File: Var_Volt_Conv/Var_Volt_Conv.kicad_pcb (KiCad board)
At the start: 2 copper layers, 99 parts, among them J101 Jack-DC, J102 Screw_Terminal_01x02, J103 Screw_Terminal_01x02, J201 Conn_01x05, Q101 AO3416, Q102 IRFML8244TRPBF, Q103 IRFML8244TRPBF, Q104 AO3407, Q105 AO3407, Q106 AO3407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

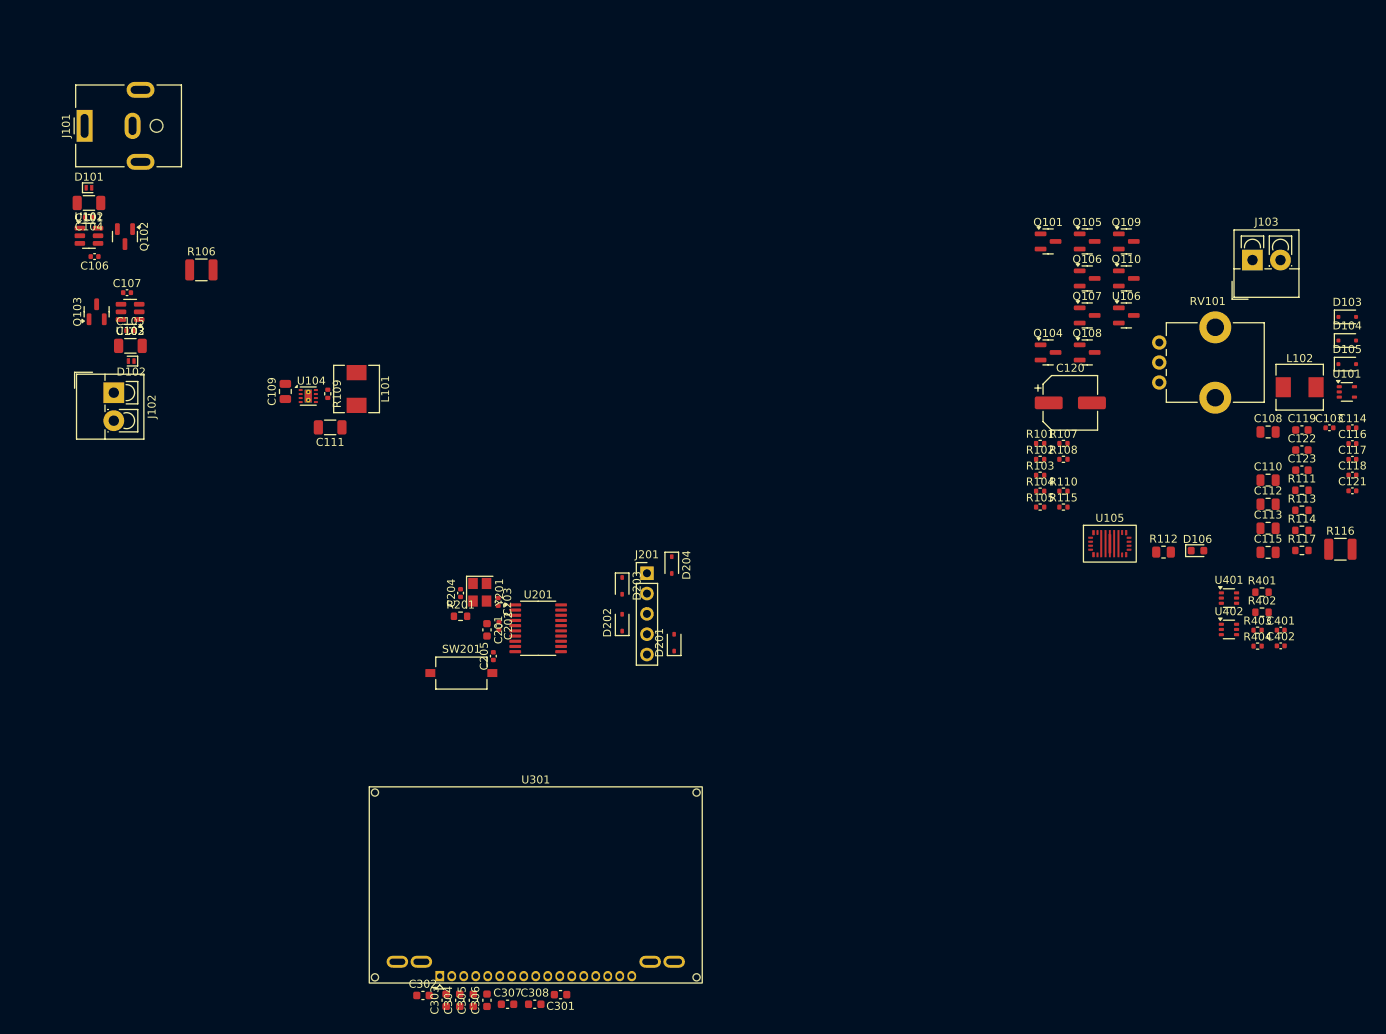
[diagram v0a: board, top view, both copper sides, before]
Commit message: Completed rough layout
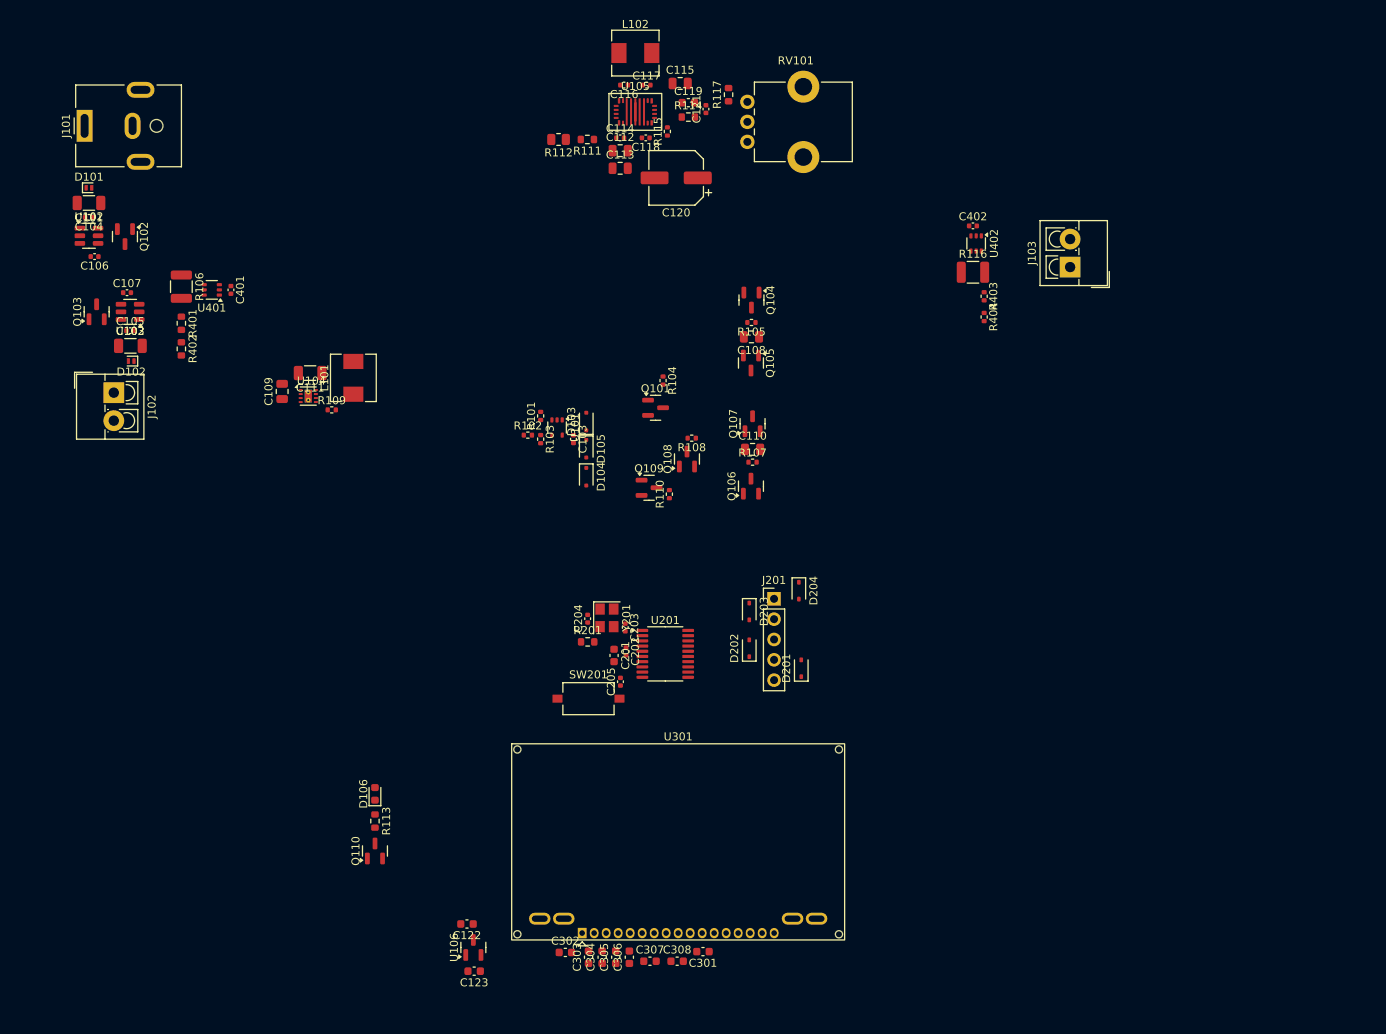
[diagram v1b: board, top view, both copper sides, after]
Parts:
- moved R401 139.2 mm to (39.0, 58.4), turned to -90 degrees
- moved R402 139.0 mm to (39.0, 61.6), turned to -90 degrees
- moved C401 137.9 mm to (45.2, 54.2), turned to -90 degrees
- moved U401 132.9 mm to (42.8, 54.2), turned to 180 degrees
- moved R113 122.2 mm to (63.2, 120.6), turned to -90 degrees
- moved C123 120.9 mm to (75.6, 139.4), turned to 180 degrees
- moved C122 120.0 mm to (74.7, 133.5), turned to 180 degrees
- moved Q110 118.1 mm to (63.2, 124.3), turned to 90 degrees
- moved U106 113.6 mm to (75.5, 136.4), turned to 90 degrees
- moved D106 107.2 mm to (63.2, 117.2), turned to 90 degrees
- moved C116 101.5 mm to (94.3, 28.6), turned to 180 degrees
- moved C117 99.9 mm to (97.2, 28.6)
- moved R111 99.5 mm to (89.8, 35.4), turned to 180 degrees
- moved U101 98.8 mm to (86.0, 71.4), turned to -90 degrees
- moved C114 98.4 mm to (93.8, 35.2)
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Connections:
- net /[1] Power/BUCK_3V3 renamed /[1] Power/BUCK_VOS
- net Net-(C121-Pad1) renamed /[1] Power/BB_COMP2
- net Net-(D103-K) renamed /[1] Power/COMP_POWER
- net Net-(D104-K) renamed /[1] Power/ST_3V3_Diode
- net Net-(D106-K) renamed /[1] Power/POW_IND_LED_R
- net Net-(Q101-D) renamed /[1] Power/BUCK_PPM_INV
- net Net-(Q104-G) renamed /[1] Power/BUCK_PPM_GATE
- net Net-(Q104-S) renamed /[1] Power/BUCK_PPM_SOURCE
- net Net-(Q106-G) renamed /[1] Power/ST_PPM_GATE
- net Net-(Q106-S) renamed /[1] Power/ST_PPM_SOURCE
- net Net-(Q108-D) renamed /[1] Power/ST_PPM_INV2
- net Net-(Q108-G) renamed /[1] Power/ST_PPM_INV1
- net Net-(Q110-D) renamed /[1] Power/POW_IND_R_NMOS
- net Net-(R111-Pad2) renamed /[1] Power/BB_FSW2
- net Net-(R117-Pad1) renamed /[1] Power/BB_POT_R
- net Net-(U101--) renamed /[1] Power/ST_PPM_IN
- net Net-(U102-VCAP) renamed /[1] Power/VCAP_J
- net Net-(U103-VCAP) renamed /[1] Power/VCAP_T
- net Net-(U104-PG) renamed /[1] Power/PG
- net Net-(U104-SW) renamed /[1] Power/BUCK_SW
- net Net-(U105-BOOT1) renamed /[1] Power/BB_BOOT1
- net Net-(U105-BOOT2) renamed /[1] Power/BB_BOOT2
- net Net-(U105-COMP) renamed /[1] Power/BB_COMP1
- net Net-(U105-FB) renamed /[1] Power/BB_FEEDBACK
- net Net-(U105-FSW) renamed /[1] Power/BB_FSW1
- net Net-(U105-SW1) renamed /[1] Power/BB_SW1
- net Net-(U105-SW2) renamed /[1] Power/BB_SW2
- net Net-(U201-PC14/PB9) renamed /[2] Microcontroller/HSE_IN
- net Net-(U301-C1+) renamed /[3] Display/LC1+
- net Net-(U301-C1-) renamed /[3] Display/LC1-
- net Net-(U301-C2+) renamed /[3] Display/LC2+
- net Net-(U301-C2-) renamed /[3] Display/LC2-
- net Net-(U301-V0) renamed /[3] Display/LV0
- net Net-(U301-V1) renamed /[3] Display/LV1
- net Net-(U301-V2) renamed /[3] Display/LV2
- net Net-(U301-V3) renamed /[3] Display/LV3
- net Net-(U301-V4) renamed /[3] Display/LV4
- net Net-(U301-VOUT) renamed /[3] Display/LVOUT
- C111 pad 2: Net-(U104-FB) -> GND
- C204 pad 2: Net-(C204-Pad2) -> /[2] Microcontroller/HSE_OUT
- U104 pad 5: Net-(U104-FB) -> GND
- U201 pad 3: Net-(U201-PC15) -> /[2] Microcontroller/HSE_OUT
- Y201 pad 1: Net-(C204-Pad2) -> /[2] Microcontroller/HSE_OUT

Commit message: Update design rules
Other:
- copper layers 2 -> 6
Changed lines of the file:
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@@
 	(generator_version "8.0")
 	(general
-		(thickness 1.6)
+		(thickness 1.5596)
 		(legacy_teardrops no)
 	)
@@
 	(layers
 		(0 "F.Cu" signal)
+		(1 "In1.Cu" power)
+		(2 "In2.Cu" power)
+		(3 "In3.Cu" power)
+		(4 "In4.Cu" power)
 		(31 "B.Cu" signal)
 		(32 "B.Adhes" user "B.Adhesive")
@@
 	)
 	(setup
+		(stackup
+			(layer "F.SilkS"
+				(type "Top Silk Screen")
+			)
+			(layer "F.Paste"
+				(type "Top Solder Paste")
+			)
+			(layer "F.Mask"
+				(type "Top Solder Mask")
+				(thickness 0.01)
+			)
+			(layer "F.Cu"
+				(type "copper")
+				(thickness 0.035)
+			)
+			(layer "dielectric 1"
+				(type "prepreg")
+				(thickness 0.1)
+				(material "FR4")
+				(epsilon_r 4.5)
+				(loss_tangent 0.02)
+			)
+			(layer "In1.Cu"
+				(type "copper")
+				(thickness 0.0152)
+			)
+			(layer "dielectric 2"
+				(type "core")
+				(thickness 0.55)
+				(material "FR4")
+				(epsilon_r 4.5)
+				(loss_tangent 0.02)
+			)
+			(layer "In2.Cu"
+				(type "copper")
+				(thickness 0.0152)
+			)
+			(layer "dielectric 3"
+				(type "prepreg")
+				(thickness 0.1088)
+				(material "FR4")
+				(epsilon_r 4.5)
+				(loss_tangent 0.02)
+			)
+			(layer "In3.Cu"
+				(type "copper")
+				(thickness 0.0152)
+			)
+			(layer "dielectric 4"
+				(type "core")
+				(thickness 0.55)
+				(material "FR4")
+				(epsilon_r 4.5)
+				(loss_tangent 0.02)
+			)
+			(layer "In4.Cu"
+				(type "copper")
+				(thickness 0.0152)
+			)
+			(layer "dielectric 5"
+				(type "prepreg")
+				(thickness 0.1)
+				(material "FR4")
+				(epsilon_r 4.5)
+				(loss_tangent 0.02)
+			)
+			(layer "B.Cu"
+				(type "copper")
+				(thickness 0.035)
+			)
+			(layer "B.Mask"
+				(type "Bottom Solder Mask")
+				(thickness 0.01)
+			)
+			(layer "B.Paste"
+				(type "Bottom Solder Paste")
+			)
+			(layer "B.SilkS"
+				(type "Bottom Silk Screen")
+			)
+			(copper_finish "None")
+			(dielectric_constraints no)
+		)
 		(pad_to_mask_clearance 0)
 		(allow_soldermask_bridges_in_footprints no)
@@
 		(tags "resistor")
 		(property "Reference" "R116"
-			(at 0 -2.28 360)
+			(at 0 -2.28 0)
 			(layer "F.SilkS")
 			(effects
@@
 		)
 		(property "Value" "11mR"
-			(at 0 2.28 360)
+			(at 0 2.28 0)
 			(layer "F.Fab")
 			(effects
@@
 		)
 		(fp_text user "${REFERENCE}"
-			(at 0 0 360)
+			(at 0 0 0)
 			(layer "F.Fab")
 			(effects
@@
 		(tags "capacitor")
 		(property "Reference" "C116"
-			(at 0 -1.16 360)
+			(at 0 -1.16 0)
 			(layer "F.SilkS")
 			(effects
@@
 		)
 		(property "Value" "0.1uF"
-			(at 0 1.16 360)
+			(at 0 1.16 0)
 			(layer "F.Fab")
 			(effects
@@
 		)
 		(fp_text user "${REFERENCE}"
-			(at 0 0 360)
+			(at 0 0 0)
 			(layer "F.Fab")
 			(effects
@@
 		(tags "capacitor")
 		(property "Reference" "C402"
-			(at 0 -1.16 360)
+			(at 0 -1.16 0)
 			(layer "F.SilkS")
 			(effects
@@
 		)
 		(property "Value" "0.1uF"
-			(at 0 1.16 360)
+			(at 0 1.16 0)
 			(layer "F.Fab")
 			(effects
@@
 		)
 		(fp_text user "${REFERENCE}"
-			(at 0 0 360)
+			(at 0 0 0)
 			(layer "F.Fab")
 			(effects
@@
 			(size 4 4)
 			(drill 2.2)
-			(layers "F&B.Cu" "*.Mask")
+			(layers "*.Cu" "*.Mask")
 		)
 		(pad "" np_thru_hole circle
@@
 			(size 4 4)
 			(drill 2.2)
-			(layers "F&B.Cu" "*.Mask")
+			(layers "*.Cu" "*.Mask")
 		)
 		(pad "1" thru_hole circle
@@
 		(tags "capacitor electrolytic")
 		(property "Reference" "C120"
-			(at 0 -4.35 360)
+			(at 0 -4.35 0)
 			(layer "F.SilkS")
 			(effects
@@
 		)
 		(property "Value" "100uF"
-			(at 0 4.35 360)
+			(at 0 4.35 0)
 			(layer "F.Fab")
 			(effects
@@
 		)
 		(fp_text user "${REFERENCE}"
-			(at 0 0 360)
+			(at 0 0 0)
 			(layer "F.Fab")
 			(effects
@@
 		(tags "capacitor")
 		(property "Reference" "C118"
-			(at 0 -1.16 360)
+			(at 0 -1.16 0)
 			(layer "F.SilkS")
 			(effects
@@
 		)
 		(property "Value" "0.1uF"
-			(at 0 1.16 360)
+			(at 0 1.16 0)
 			(layer "F.Fab")
 			(effects
@@
 		)
 		(fp_text user "${REFERENCE}"
-			(at 0 0 360)
+			(at 0 0 0)
 			(layer "F.Fab")
 			(effects
@@
 		)
 		(fp_text user "${REFERENCE}"
-			(at 0 0 360)
+			(at 0 0 0)
 			(layer "F.Fab")
 			(effects
@@
 		(tags "SOT TO_SOT_SMD")
 		(property "Reference" "Q101"
-			(at 0 -2.4 360)
+			(at 0 -2.4 0)
 			(layer "F.SilkS")
 			(effects
@@
 		)
 		(property "Value" "AO3416"
-			(at 0 2.4 360)
+			(at 0 2.4 0)
 			(layer "F.Fab")
 			(effects
@@
 		)
 		(fp_text user "${REFERENCE}"
-			(at 0 0 360)
+			(at 0 0 0)
 			(layer "F.Fab")
 			(effects
@@
 		(tags "resistor")
 		(property "Reference" "R112"
-			(at 0 -1.65 360)
+			(at 0 -1.65 0)
 			(layer "F.SilkS")
 			(effects
@@
 		)
 		(property "Value" "4.3k"
-			(at 0 1.65 360)
+			(at 0 1.65 0)
 			(layer "F.Fab")
 			(effects
@@
 		)
 		(fp_text user "${REFERENCE}"
-			(at 0 0 360)
+			(at 0 0 0)
 			(layer "F.Fab")
 			(effects
@@
 		(tags "capacitor")
 		(property "Reference" "C110"
-			(at 0 -1.68 360)
+			(at 0 -1.68 0)
 			(layer "F.SilkS")
 			(effects
@@
 		)
 		(property "Value" "10uF"
-			(at 0 1.68 360)
+			(at 0 1.68 0)
 			(layer "F.Fab")
 			(effects
@@
 		)
 		(fp_text user "${REFERENCE}"
-			(at 0 0 360)
+			(at 0 0 0)
 			(layer "F.Fab")
 			(effects
@@
 		(tags "resistor")
 		(property "Reference" "R108"
-			(at 0 -1.17 360)
+			(at 0 -1.17 0)
 			(layer "F.SilkS")
 			(effects
@@
 		)
 		(property "Value" "100k"
-			(at 0 1.17 360)
+			(at 0 1.17 0)
 			(layer "F.Fab")
 			(effects
@@
 		)
 		(fp_text user "${REFERENCE}"
-			(at 0 0 360)
+			(at 0 0 0)
 			(layer "F.Fab")
 			(effects
@@
 		(tags "resistor")
 		(property "Reference" "R105"
-			(at 0 -1.17 360)
+			(at 0 -1.17 0)
 			(layer "F.SilkS")
 			(effects
@@
 		)
 		(property "Value" "100k"
-			(at 0 1.17 360)
+			(at 0 1.17 0)
 			(layer "F.Fab")
 			(effects
@@
 		)
 		(fp_text user "${REFERENCE}"
-			(at 0 0 360)
+			(at 0 0 0)
 			(layer "F.Fab")
 			(effects
@@
 		(tags "capacitor")
 		(property "Reference" "C108"
-			(at 0 -1.68 360)
+			(at 0 -1.68 0)
 			(layer "F.SilkS")
 			(effects
@@
 		)
 		(property "Value" "10uF"
-			(at 0 1.68 360)
+			(at 0 1.68 0)
 			(layer "F.Fab")
 			(effects
@@
 		)
 		(fp_text user "${REFERENCE}"
-			(at 0 0 360)
+			(at 0 0 0)
 			(layer "F.Fab")
 			(effects
@@
 		(tags "SOT-363 SC-70-6")
 		(property "Reference" "U401"
-			(at 0 -2.25 360)
+			(at 0 -2.25 0)
 			(layer "F.SilkS")
 			(effects
@@
 		)
 		(property "Value" "INA215BIDCKR"
-			(at 0 2 360)
+			(at 0 2 0)
 			(layer "F.Fab")
 			(effects
@@
 		(tags "resistor")
 		(property "Reference" "R107"
-			(at 0 -1.17 360)
+			(at 0 -1.17 0)
 			(layer "F.SilkS")
 			(effects
@@
 		)
 		(property "Value" "100k"
-			(at 0 1.17 360)
+			(at 0 1.17 0)
 			(layer "F.Fab")
 			(effects
@@
 		)
 		(fp_text user "${REFERENCE}"
-			(at 0 0 360)
+			(at 0 0 0)
 			(layer "F.Fab")
 			(effects
@@
 		(tags "capacitor")
 		(property "Reference" "C117"
-			(at 0 -1.16 360)
+			(at 0 -1.16 0)
 			(layer "F.SilkS")
 			(effects
@@
 		)
 		(property "Value" "0.1uF"
-			(at 0 1.16 360)
+			(at 0 1.16 0)
 			(layer "F.Fab")
 			(effects
@@
 		)
 		(fp_text user "${REFERENCE}"
-			(at 0 0 360)
+			(at 0 0 0)
 			(layer "F.Fab")
 			(effects
@@
 		(tags "resistor")
 		(property "Reference" "R111"
-			(at 0 -1.43 360)
+			(at 0 -1.43 0)
 			(layer "F.SilkS")
 			(effects
@@
 		)
 		(property "Value" "5k"
-			(at 0 1.43 360)
+			(at 0 1.43 0)
 			(layer "F.Fab")
 			(effects
@@
 		)
 		(fp_text user "${REFERENCE}"
-			(at 0 0 360)
+			(at 0 0 0)
 			(layer "F.Fab")
 			(effects

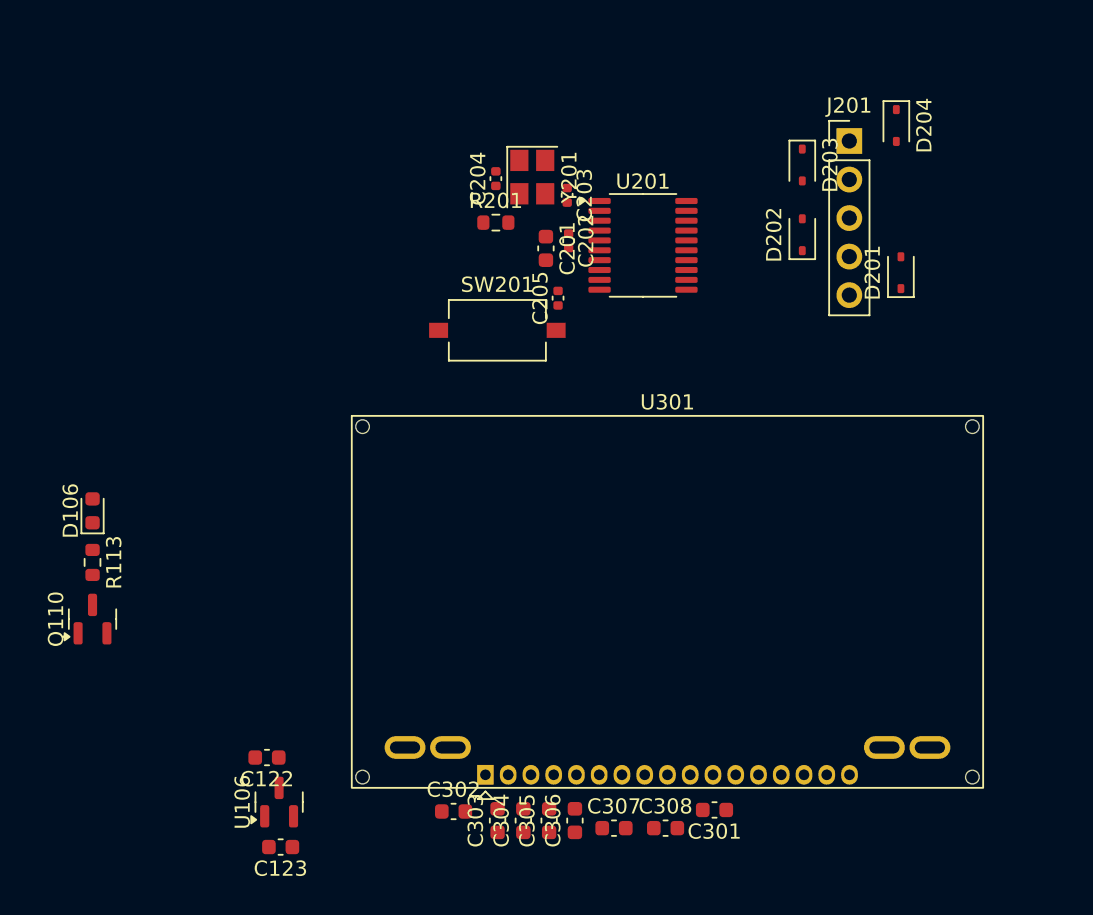
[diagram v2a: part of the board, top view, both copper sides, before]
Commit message: Routed signal traces and made power pours for microcontroller and display, also changed 4.7, 1uF and 2.2uF caps to 0402
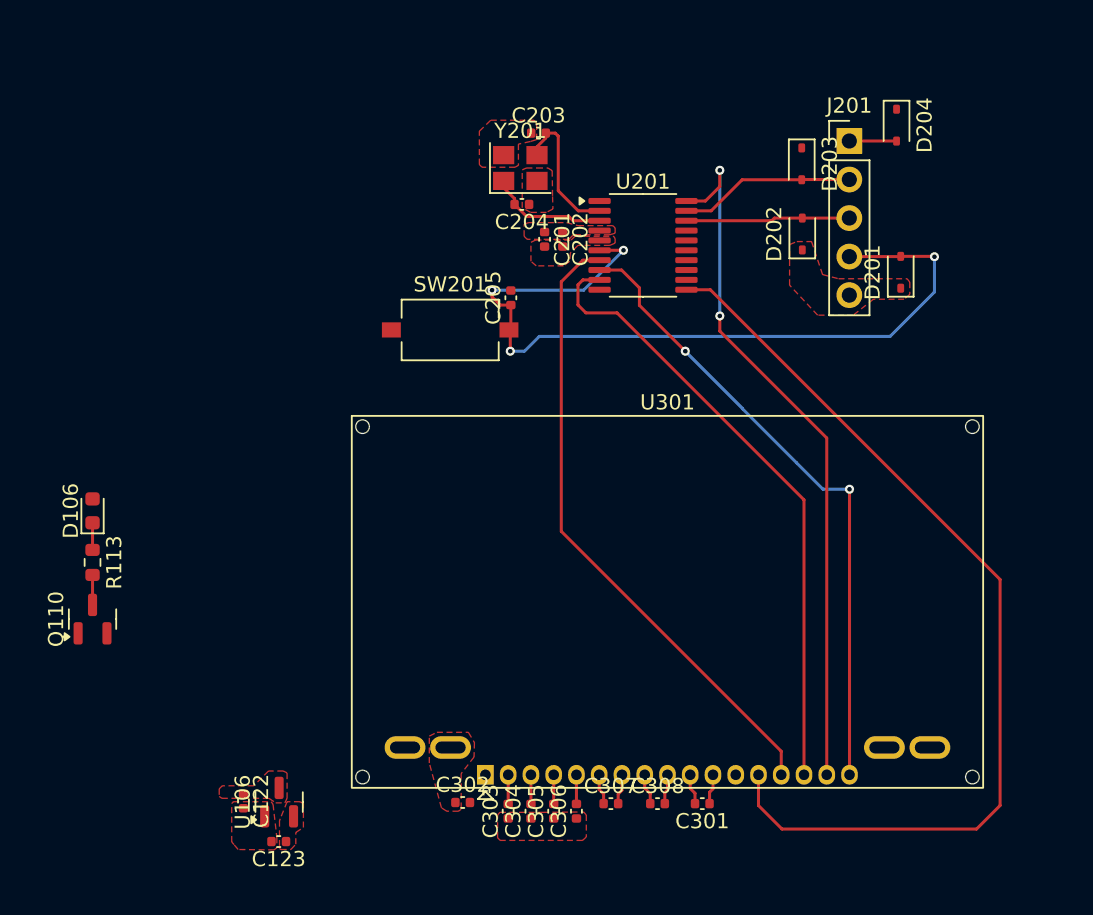
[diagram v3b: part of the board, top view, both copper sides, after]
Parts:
- removed R201: 0R, Resistor_SMD:R_0603_1608Metric
- C122, C123, C201, C301, C302, C303, C304, C305, C306, C307, C308: footprint Capacitor_SMD:C_0603_1608Metric -> Capacitor_SMD:C_0402_1005Metric
- moved C203 4.51 mm to (92.6, 92.3), turned to 0 degrees
- moved C122 3.26 mm to (73.2, 136.3), turned to -90 degrees
- moved C205 3.11 mm to (90.8, 103.2)
- moved SW201 3.11 mm to (86.8, 105.3)
- moved C204 2.41 mm to (91.5, 97.0), turned to 180 degrees
- moved C308 1.70 mm to (100.4, 136.5)
- moved C307 1.63 mm to (97.4, 136.5)
- moved Y201 0.99 mm to (91.4, 94.6), turned to 0 degrees
- moved C303 0.93 mm to (90.6, 137.0)
- moved C301 0.91 mm to (103.4, 136.5)
- moved C302 0.84 mm to (87.6, 136.4)
- moved C304 0.79 mm to (92.1, 137.0)
- moved C305 0.69 mm to (93.6, 137.0)
- moved C306 0.63 mm to (95.1, 137.0)
- moved C201 0.61 mm to (93.0, 99.3)
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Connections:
- D202 pad 2: /[2] Microcontroller/SWCLK -> /[2] Microcontroller/SWDIO
- D203 pad 2: /[2] Microcontroller/SWDIO -> /[2] Microcontroller/SWCLK
- J201 pad 2: /[2] Microcontroller/SWDIO -> /[2] Microcontroller/SWCLK
- J201 pad 3: /[2] Microcontroller/SWCLK -> /[2] Microcontroller/SWDIO
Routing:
- net SPI_MOSI: track 0.00 -> 62.7 mm
- net /[2] Microcontroller/NRST: track 0.00 -> 53.9 mm, vias 0 -> 4
- net /RESET: track 0.00 -> 46.4 mm, vias 0 -> 2
- net /CHIP_SELECT: track 0.00 -> 42.0 mm, vias 0 -> 2
- net SPI_CLK: track 0.00 -> 41.6 mm
- net REGISTER_SELECT: track 0.00 -> 41.2 mm
- net /[2] Microcontroller/SWCLK: track 0.00 -> 11.6 mm
- net /[2] Microcontroller/SWDIO: track 0.00 -> 10.8 mm
- net /[2] Microcontroller/HSE_IN: track 0.00 -> 9.47 mm
- net /[2] Microcontroller/HSE_OUT: track 0.00 -> 7.90 mm
- net ST_3V3: track 0.00 -> 3.11 mm
- net /[3] Display/LC1+: track 0.00 -> 2.05 mm
- net /[3] Display/LVOUT: track 0.00 -> 2.03 mm
- net /[3] Display/LC2-: track 0.00 -> 2.02 mm
- net /[3] Display/LC2+: track 0.00 -> 2.00 mm
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- added copper zone on F.Cu, net +3V0
- added copper zone on F.Cu, net +3V3
- added copper zone on F.Cu, net GND
